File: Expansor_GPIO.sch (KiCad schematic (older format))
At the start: 6 parts, among them U6 MCP23017, U7 MCP23017

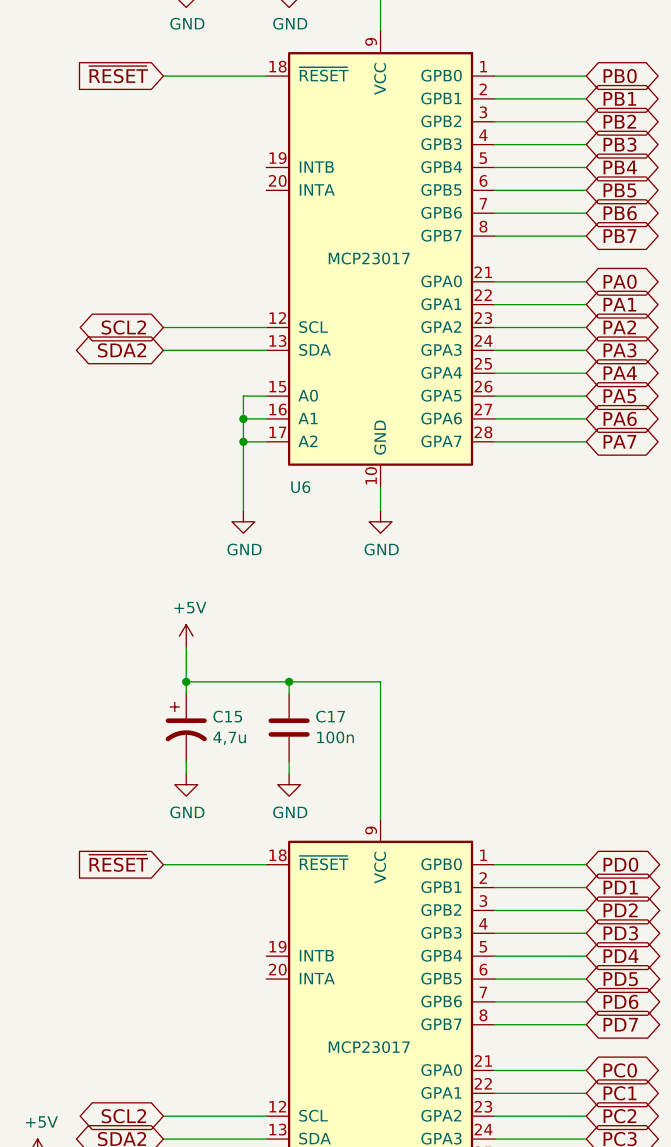
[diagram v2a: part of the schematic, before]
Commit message: cambiar ch340T por ch340g y añadir nc a pines
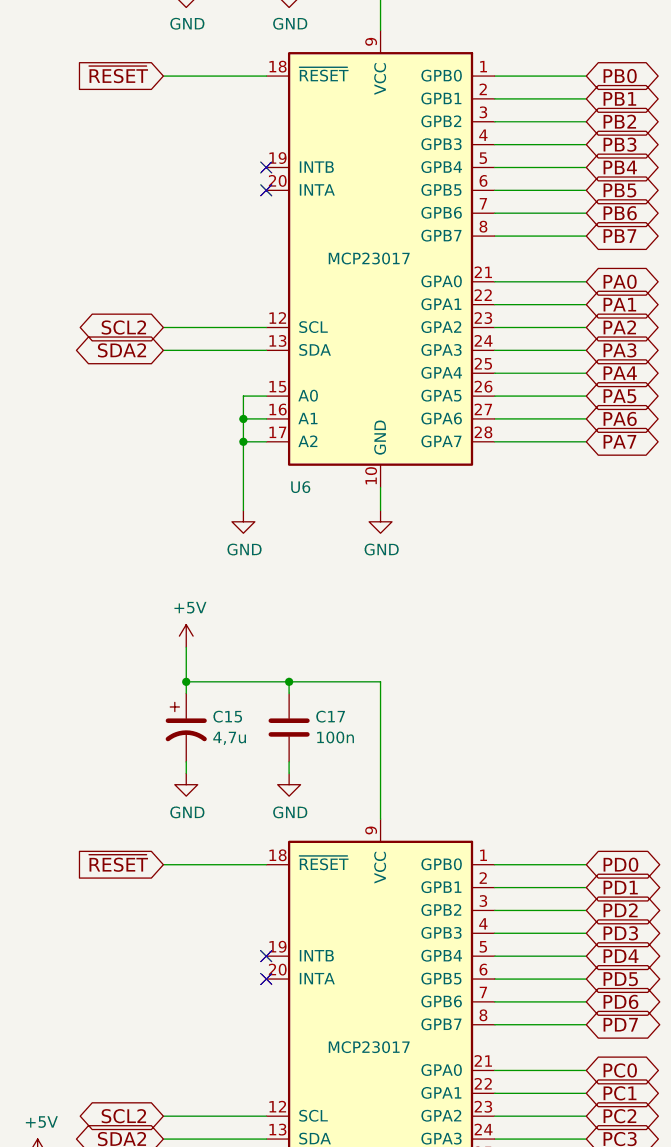
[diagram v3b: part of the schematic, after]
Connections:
- no-connect marks 0 -> 4
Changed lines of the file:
@@
 $Descr A4 11693 8268
 encoding utf-8
-Sheet 5 15
+Sheet 5 14
 Title ""
 Date "2017-01-15"
@@
 $EndComp
 $Comp
-L GND #PWR044
+L GND #PWR052
 U 1 1 587AB8C8
 P 3300 3900
-F 0 "#PWR044" H 3300 3650 50  0001 C CNN
+F 0 "#PWR052" H 3300 3650 50  0001 C CNN
 F 1 "GND" H 3305 3727 50  0000 C CNN
 F 2 "" H 3300 3900 50  0000 C CNN
@@
 	3300 3900 3300 3800
 $Comp
-L GND #PWR045
+L GND #PWR053
 U 1 1 587AB8EE
 P 2700 3900
-F 0 "#PWR045" H 2700 3650 50  0001 C CNN
+F 0 "#PWR053" H 2700 3650 50  0001 C CNN
 F 1 "GND" H 2705 3727 50  0000 C CNN
 F 2 "" H 2700 3900 50  0000 C CNN
@@
 	2450 1050 2450 1250
 $Comp
-L GND #PWR046
+L GND #PWR054
 U 1 1 587ABE16
 P 2450 1600
-F 0 "#PWR046" H 2450 1350 50  0001 C CNN
+F 0 "#PWR054" H 2450 1350 50  0001 C CNN
 F 1 "GND" H 2455 1427 50  0000 C CNN
 F 2 "" H 2450 1600 50  0000 C CNN
@@
 Connection ~ 2900 1200
 $Comp
-L GND #PWR047
+L GND #PWR055
 U 1 1 587ABE80
 P 2900 1600
-F 0 "#PWR047" H 2900 1350 50  0001 C CNN
+F 0 "#PWR055" H 2900 1350 50  0001 C CNN
 F 1 "GND" H 2905 1427 50  0000 C CNN
 F 2 "" H 2900 1600 50  0000 C CNN
@@
 $EndComp
 $Comp
-L +5V #PWR048
+L +5V #PWR056
 U 1 1 587ABF96
 P 2450 1050
-F 0 "#PWR048" H 2450 900 50  0001 C CNN
+F 0 "#PWR056" H 2450 900 50  0001 C CNN
 F 1 "+5V" H 2465 1223 50  0000 C CNN
 F 2 "" H 2450 1050 50  0000 C CNN
@@
 $EndComp
 $Comp
-L GND #PWR049
+L GND #PWR057
 U 1 1 587C5572
 P 3300 7350
-F 0 "#PWR049" H 3300 7100 50  0001 C CNN
+F 0 "#PWR057" H 3300 7100 50  0001 C CNN
 F 1 "GND" H 3305 7177 50  0000 C CNN
 F 2 "" H 3300 7350 50  0000 C CNN
@@
 	3300 7350 3300 7250
 $Comp
-L GND #PWR050
+L GND #PWR058
 U 1 1 587C5579
 P 2700 7350
-F 0 "#PWR050" H 2700 7100 50  0001 C CNN
+F 0 "#PWR058" H 2700 7100 50  0001 C CNN
 F 1 "GND" H 2705 7177 50  0000 C CNN
 F 2 "" H 2700 7350 50  0000 C CNN
@@
 	2450 4500 2450 4700
 $Comp
-L GND #PWR051
+L GND #PWR059
 U 1 1 587C55A2
 P 2450 5050
-F 0 "#PWR051" H 2450 4800 50  0001 C CNN
+F 0 "#PWR059" H 2450 4800 50  0001 C CNN
 F 1 "GND" H 2455 4877 50  0000 C CNN
 F 2 "" H 2450 5050 50  0000 C CNN
@@
 Connection ~ 2900 4650
 $Comp
-L GND #PWR052
+L GND #PWR060
 U 1 1 587C55AC
 P 2900 5050
-F 0 "#PWR052" H 2900 4800 50  0001 C CNN
+F 0 "#PWR060" H 2900 4800 50  0001 C CNN
 F 1 "GND" H 2905 4877 50  0000 C CNN
 F 2 "" H 2900 5050 50  0000 C CNN
@@
 $EndComp
 $Comp
-L +5V #PWR053
+L +5V #PWR061
 U 1 1 587C55B2
 P 2450 4500
-F 0 "#PWR053" H 2450 4350 50  0001 C CNN
+F 0 "#PWR061" H 2450 4350 50  0001 C CNN
 F 1 "+5V" H 2465 4673 50  0000 C CNN
 F 2 "" H 2450 4500 50  0000 C CNN
@@
 	1800 6950 1800 6750
 $Comp
-L +5V #PWR054
+L +5V #PWR062
 U 1 1 5891285D
 P 1800 6750
-F 0 "#PWR054" H 1800 6600 50  0001 C CNN
+F 0 "#PWR062" H 1800 6600 50  0001 C CNN
 F 1 "+5V" H 1815 6923 50  0000 C CNN
 F 2 "" H 1800 6750 50  0001 C CNN
@@
 	1    0    0    -1
 $EndComp
+NoConn ~ 2800 2400
+NoConn ~ 2800 2500
+NoConn ~ 2800 5850
+NoConn ~ 2800 5950
 $EndSCHEMATC

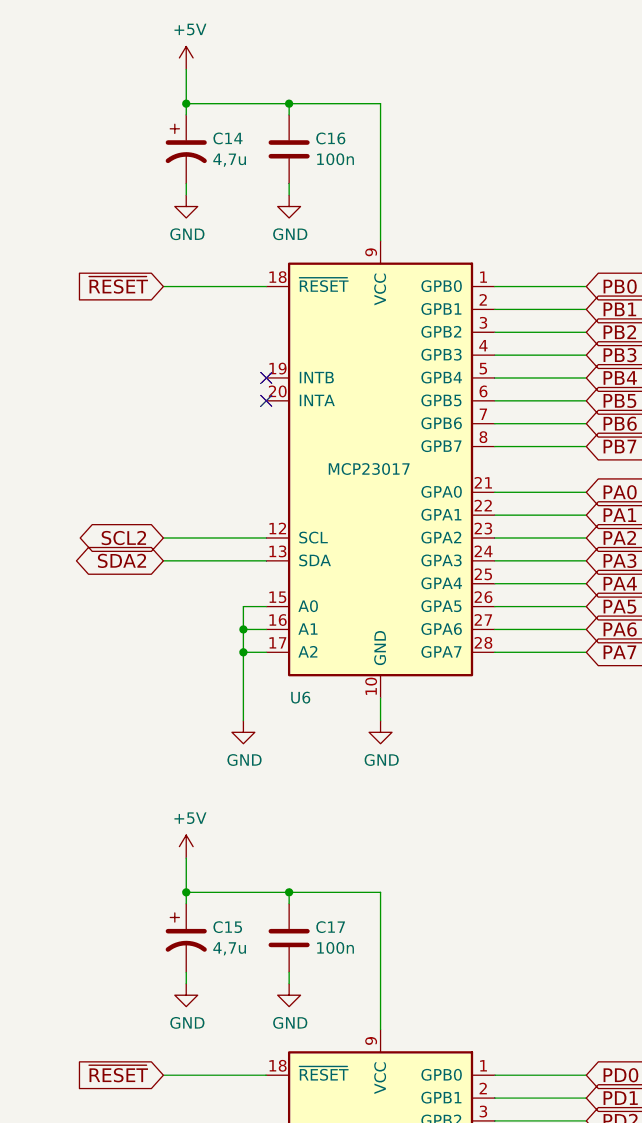
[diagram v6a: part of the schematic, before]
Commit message: añadidos valores y referencias a control, alimentacion y gpioEx
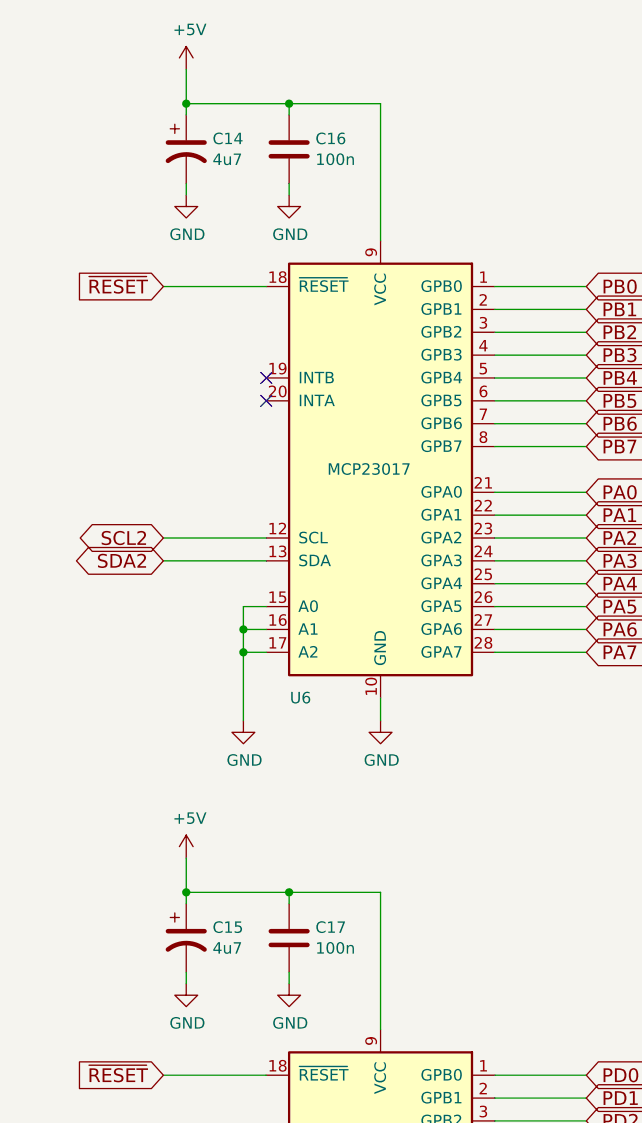
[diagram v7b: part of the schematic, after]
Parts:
- C14, C15: value 4,7u -> 4u7; Fabricante (none) -> SAMSUNG; Provedor (none) -> TME; Ref (none) -> CL31F475ZOFNNNE; Ref_Proveedor (none) -> CL31F475ZOFNNNE
- C16, C17: Fabricante (none) -> SAMSUNG; Provedor (none) -> TME; Ref (none) -> CL21B104KBCNNNC; Ref_Proveedor (none) -> CL21B104KBCNNNC
- U6, U7: Provedor tme -> rs; Ref MCP23017-E/SO -> MCP23017-E/SS; Ref_Proveedor MCP23017-E/SO -> 681-1128
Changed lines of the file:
@@
 F 3 "" H 3550 3800 50  0001 C CNN
 F 4 "MICROCHIP TECHNOLOGY" H 3300 2800 60  0001 C CNN "Fabricante"
-F 5 "MCP23017-E/SO" H 3300 2800 60  0001 C CNN "Ref"
+F 5 "MCP23017-E/SS" H 3300 2800 60  0001 C CNN "Ref"
 F 6 "~" H 3300 2800 60  0001 C CNN "Potencia"
 F 7 "~" H 3300 2800 60  0001 C CNN "Tolerancia"
-F 8 "tme" H 3300 2800 60  0001 C CNN "Provedor"
-F 9 "MCP23017-E/SO" H 3300 2800 60  0001 C CNN "Ref_Proveedor"
+F 8 "rs" H 3300 2800 60  0001 C CNN "Provedor"
+F 9 "681-1128" H 3300 2800 60  0001 C CNN "Ref_Proveedor"
 	1    3300 2800
 	-1   0    0    -1
@@
 P 2450 1400
 F 0 "C14" H 2565 1446 50  0000 L CNN
-F 1 "4,7u" H 2565 1355 50  0000 L CNN
+F 1 "4u7" H 2565 1355 50  0000 L CNN
 F 2 "Capacitors_SMD:C_1206" H 2450 1400 50  0001 C CNN
 F 3 "" H 2450 1400 50  0000 C CNN
+F 4 "SAMSUNG" H 1650 1750 60  0001 C CNN "Fabricante"
+F 5 "CL31F475ZOFNNNE" H 1650 1750 60  0001 C CNN "Ref"
+F 6 "~" H 1650 1750 60  0001 C CNN "Potencia"
+F 7 "~" H 1650 1750 60  0001 C CNN "Tolerancia"
+F 8 "TME" H 1650 1750 60  0001 C CNN "Provedor"
+F 9 "CL31F475ZOFNNNE" H 1650 1750 60  0001 C CNN "Ref_Proveedor"
 	1    2450 1400
 	1    0    0    -1
@@
 F 2 "Capacitors_SMD:C_0805" H 2938 1250 50  0001 C CNN
 F 3 "" H 2900 1400 50  0000 C CNN
+F 4 "SAMSUNG" H 7000 1050 60  0001 C CNN "Fabricante"
+F 5 "CL21B104KBCNNNC" H 7000 1050 60  0001 C CNN "Ref"
+F 6 "~" H 7000 1050 60  0001 C CNN "Potencia"
+F 7 "~" H 7000 1050 60  0001 C CNN "Tolerancia"
+F 8 "TME" H 7000 1050 60  0001 C CNN "Provedor"
+F 9 "CL21B104KBCNNNC" H 7000 1050 60  0001 C CNN "Ref_Proveedor"
 	1    2900 1400
 	1    0    0    -1
@@
 F 3 "" H 3550 7250 50  0001 C CNN
 F 4 "MICROCHIP TECHNOLOGY" H 3300 6250 60  0001 C CNN "Fabricante"
-F 5 "MCP23017-E/SO" H 3300 6250 60  0001 C CNN "Ref"
+F 5 "MCP23017-E/SS" H 3300 6250 60  0001 C CNN "Ref"
 F 6 "~" H 3300 6250 60  0001 C CNN "Potencia"
 F 7 "~" H 3300 6250 60  0001 C CNN "Tolerancia"
-F 8 "tme" H 3300 6250 60  0001 C CNN "Provedor"
-F 9 "MCP23017-E/SO" H 3300 6250 60  0001 C CNN "Ref_Proveedor"
+F 8 "rs" H 3300 6250 60  0001 C CNN "Provedor"
+F 9 "681-1128" H 3300 6250 60  0001 C CNN "Ref_Proveedor"
 	1    3300 6250
 	-1   0    0    -1
@@
 P 2450 4850
 F 0 "C15" H 2565 4896 50  0000 L CNN
-F 1 "4,7u" H 2565 4805 50  0000 L CNN
+F 1 "4u7" H 2565 4805 50  0000 L CNN
 F 2 "Capacitors_SMD:C_1206" H 2450 4850 50  0001 C CNN
 F 3 "" H 2450 4850 50  0000 C CNN
+F 4 "SAMSUNG" H 1650 1750 60  0001 C CNN "Fabricante"
+F 5 "CL31F475ZOFNNNE" H 1650 1750 60  0001 C CNN "Ref"
+F 6 "~" H 1650 1750 60  0001 C CNN "Potencia"
+F 7 "~" H 1650 1750 60  0001 C CNN "Tolerancia"
+F 8 "TME" H 1650 1750 60  0001 C CNN "Provedor"
+F 9 "CL31F475ZOFNNNE" H 1650 1750 60  0001 C CNN "Ref_Proveedor"
 	1    2450 4850
 	1    0    0    -1
@@
 F 2 "Capacitors_SMD:C_0805" H 2938 4700 50  0001 C CNN
 F 3 "" H 2900 4850 50  0000 C CNN
+F 4 "SAMSUNG" H 7000 1050 60  0001 C CNN "Fabricante"
+F 5 "CL21B104KBCNNNC" H 7000 1050 60  0001 C CNN "Ref"
+F 6 "~" H 7000 1050 60  0001 C CNN "Potencia"
+F 7 "~" H 7000 1050 60  0001 C CNN "Tolerancia"
+F 8 "TME" H 7000 1050 60  0001 C CNN "Provedor"
+F 9 "CL21B104KBCNNNC" H 7000 1050 60  0001 C CNN "Ref_Proveedor"
 	1    2900 4850
 	1    0    0    -1
